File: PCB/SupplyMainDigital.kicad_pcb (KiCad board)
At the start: 2 copper layers, 84.8 x 57.5 mm, 103 parts, among them CON1 BARREL_JACK, P1 12V, P2 5V, P3 3V3, P4 GND, P5 PGM, P6 SERIAL, P7 I2C, P8 OUT, SW1 SW_PUSH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

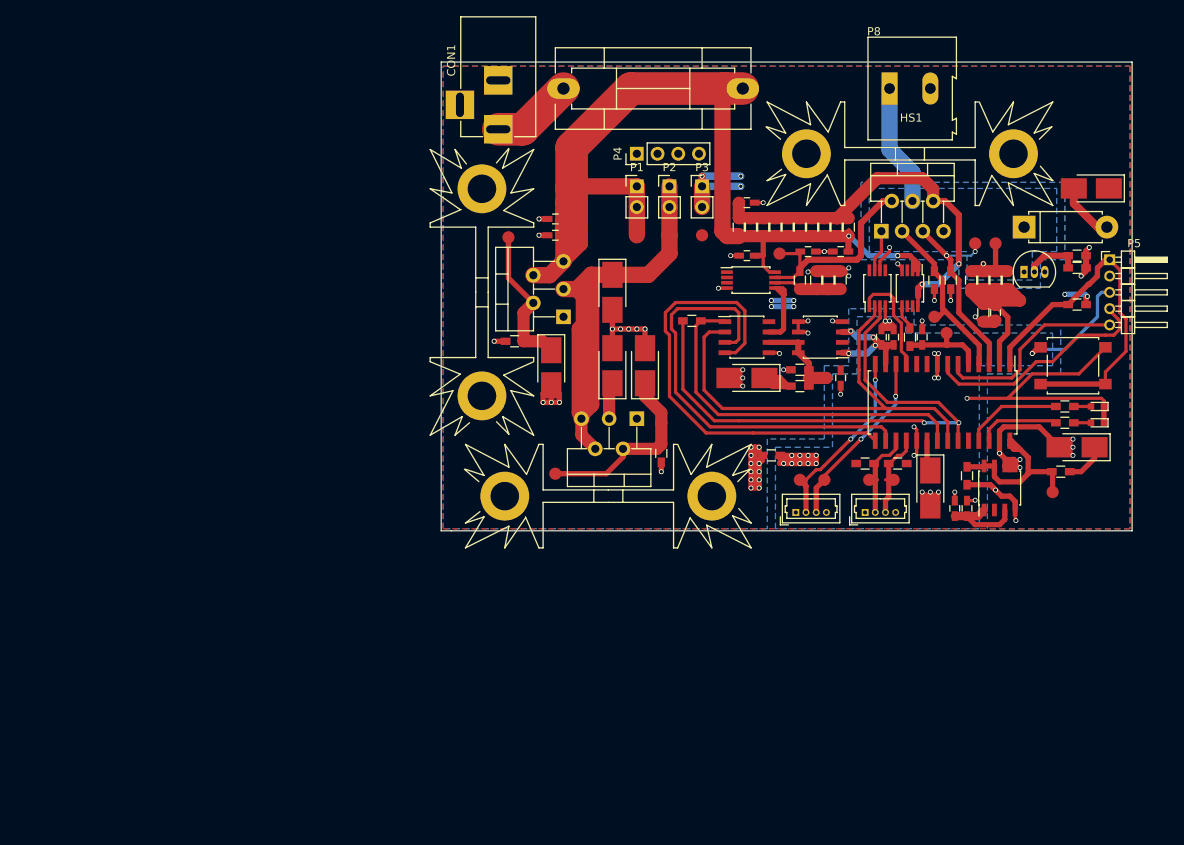
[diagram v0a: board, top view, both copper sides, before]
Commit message: component layout done
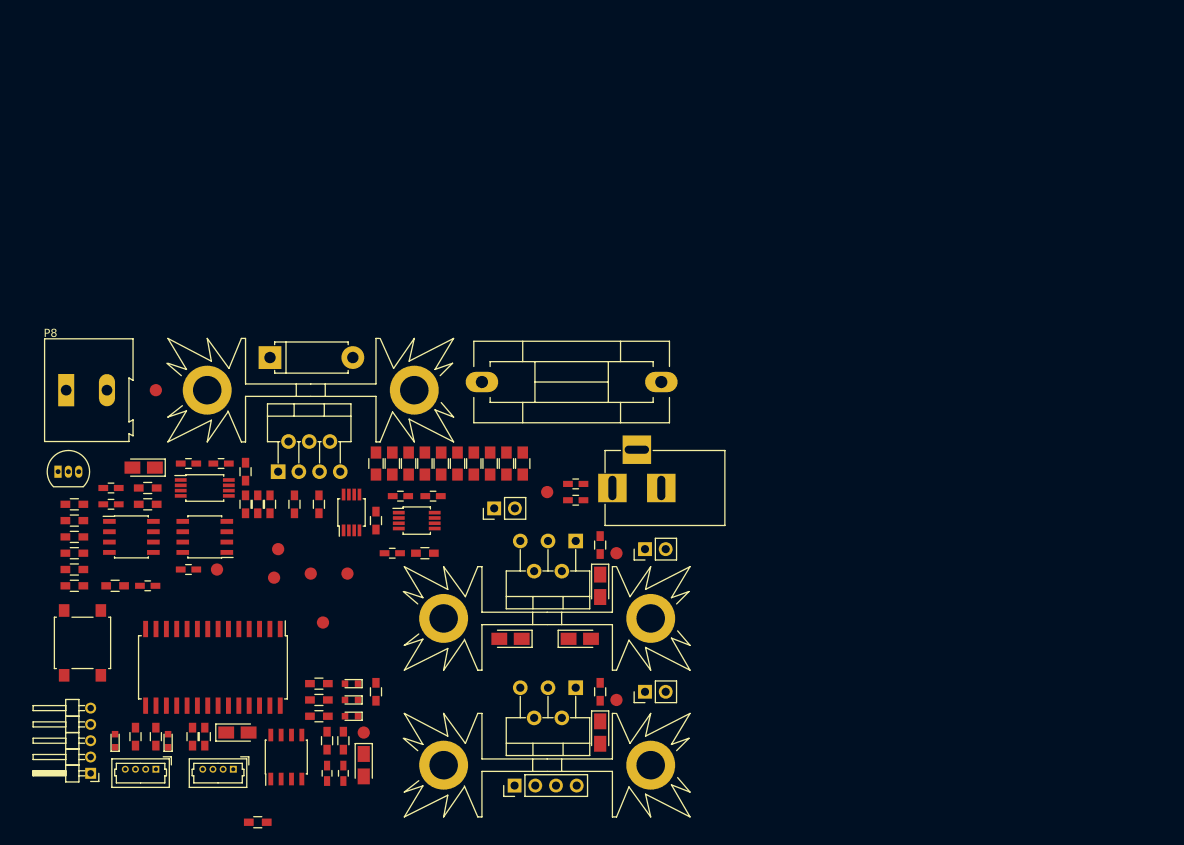
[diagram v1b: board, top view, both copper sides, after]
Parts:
- removed TP10, TP11, TP15, TP17, TP4, TP5: TEST, Measurement_Points:Measurement_Point_Round-SMD-Pad_Small
- removed eC20: 2.2µ **, Capacitors_Tantalum_SMD:CP_Tantalum_Case-B_EIA-3528-21_Hand
- added D4: LED, LEDs:LED_0603, F.Cu at (102.5, 95.0)
- added D5: LED, LEDs:LED_0603, F.Cu at (96.0, 95.0)
- added D6: LED, LEDs:LED_0603, F.Cu at (125.0, 88.0)
- added R38: 100, Resistors_SMD:R_0603_HandSoldering, F.Cu at (101.0, 94.5)
- added R39: 100, Resistors_SMD:R_0603_HandSoldering, F.Cu at (98.5, 94.5)
- added R40: 100, Resistors_SMD:R_0603_HandSoldering, F.Cu at (121.0, 88.0)
- C17, C18, C19, C20, C5, C6, C8: footprint Capacitors_Tantalum_SMD:CP_Tantalum_Case-B_EIA-3528-21_Hand -> Capacitors_Tantalum_SMD:CP_Tantalum_Case-A_EIA-3216-18_Reflow
- R14, R15, R16, R17, R18, R19, R20, R21, R22, R23: footprint Resistors_SMD:R_0603_HandSoldering -> Resistors_SMD:R_0805_HandSoldering
- TP1, TP2: value TEST -> Vref
- TP12: value TEST -> Vo+
- TP3: value TEST -> Set
- TP6: value TEST -> Vout
- TP7: value TEST -> Temp
- TP8: value TEST -> Imon
- TP9: value TEST -> Sense
- moved P5 140.0 mm to (93.0, 99.0), turned to 180 degrees
- moved R24 127.2 mm to (91.0, 68.0)
- moved R25 126.4 mm to (91.0, 66.0)
- moved SW1 126.2 mm to (92.0, 83.0), turned to 90 degrees
- moved U8 121.0 mm to (89.0, 62.0)
- moved R31 120.5 mm to (91.0, 76.0), turned to 0 degrees
- moved R29 117.9 mm to (91.0, 72.0), turned to 0 degrees
- moved R27 115.9 mm to (91.0, 70.0), turned to 0 degrees
- moved R30 115.6 mm to (91.0, 74.0), turned to 0 degrees
- moved R28 111.6 mm to (96.0, 76.0), turned to 0 degrees
- moved C14 109.3 mm to (100.0, 76.0), turned to 0 degrees
- moved P8 107.6 mm to (90.0, 52.0)
- moved C2 105.0 mm to (95.5, 66.0), turned to 0 degrees
- moved TP12 104.6 mm to (101.0, 52.0)
- moved C4 103.5 mm to (95.5, 64.0), turned to 0 degrees
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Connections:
- U5 pad 12: /SER_RX -> /SPI_CS_DAC
- U5 pad 14: /SER_TX -> /SPI_FS
- U5 pad 15: /SPI_FS -> /SER_RX
- U5 pad 16: /SPI_CS_DAC -> /SER_TX
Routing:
- net +12V: track 130.4 -> 0.00 mm, vias 2 -> 0
- net GNDA: track 119.6 -> 0.00 mm, vias 53 -> 0
- net GND: track 91.5 -> 0.00 mm, vias 25 -> 0
- net /SPI_SDI: track 69.8 -> 0.00 mm, vias 2 -> 0
- net +5V: track 60.6 -> 0.00 mm
- net /SPI_SCK: track 58.1 -> 0.00 mm
- net /SPI_FS: track 55.6 -> 0.00 mm
- net /SPI_CS_DAC: track 52.5 -> 0.00 mm
- net +3V3: track 50.1 -> 0.00 mm, vias 9 -> 0
- net /3081_IN: track 49.6 -> 0.00 mm, vias 2 -> 0
- net /SPI_SDO: track 45.3 -> 0.00 mm
- net /RESET: track 44.9 -> 0.00 mm
- net /PGM_PGED: track 28.6 -> 0.00 mm
- net /VO+: track 27.1 -> 0.00 mm, vias 2 -> 0
- net /VO_SENSE: track 26.0 -> 0.00 mm
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- removed copper zone on F.Cu, net +3V3
- removed copper zone on B.Cu, net /VO+
- removed copper zone on B.Cu, net GND
- removed copper zone on B.Cu, net GNDA
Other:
- board outline removed
- rule pad_to_mask_clearance: 0.2 -> 0
- rule trace_min: 0.1524 -> 0.2
- rule via_min_drill: 0.254 -> 0.3
- rule via_min_size: 0.381 -> 0.4

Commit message: Pcb layout V2 ready
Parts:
- TP12: value Vo+ -> Vout+
- TP6: value Vout -> Vo
- TP7: value Temp -> Sense
- TP8: value Imon -> Temp
- TP9: value Sense -> Imon
- U5: value dsPIC33EPXXXGP502 -> dsPIC33EP
- moved R36 32.9 mm to (90.5, 81.5), turned to 270 degrees
- moved SW1 31.6 mm to (123.6, 82.0), turned to 270 degrees
- moved TP6 19.3 mm to (96.5, 78.5)
- moved P4 17.4 mm to (132.0, 89.0)
- moved TP2 14.6 mm to (101.0, 61.5)
- moved TP3 14.1 mm to (109.5, 59.0)
- moved R5 13.7 mm to (118.6, 79.0), turned to 90 degrees
- moved C2 11.0 mm to (100.0, 76.0)
- moved C4 11.0 mm to (100.0, 74.0)
- moved TP7 10.7 mm to (128.2, 67.8)
- moved TP9 10.4 mm to (114.8, 71.0)
- moved TP8 10.1 mm to (118.0, 71.0)
- moved C1 7.00 mm to (117.0, 99.0)
- moved C3 7.00 mm to (115.0, 99.0)
- moved R1 7.00 mm to (115.0, 95.0)
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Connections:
- TP7 pad 1: /TEMP -> /VSENSE
- TP8 pad 1: /IMON -> /TEMP
- TP9 pad 1: /VSENSE -> /IMON
- U5 pad 3: /TEMP -> /VSENSE
- U5 pad 4: /IMON -> /TEMP
- U5 pad 5: /VSENSE -> /IMON
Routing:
- net +12V: track 0.00 -> 121.8 mm, vias 0 -> 6
- net GNDA: track 0.00 -> 105.0 mm, vias 0 -> 50
- net /VO+: track 0.00 -> 83.9 mm
- net /RESET: track 0.00 -> 82.0 mm, vias 0 -> 4
- net +5V: track 0.00 -> 81.0 mm
- net GND: track 0.00 -> 66.8 mm, vias 0 -> 24
- net /SPI_SCK: track 0.00 -> 54.3 mm, vias 0 -> 2
- net /SPI_SDO: track 0.00 -> 45.1 mm, vias 0 -> 2
- net /VO_SENSE: track 0.00 -> 39.8 mm, vias 0 -> 2
- net /SPI_CS_MCP: track 0.00 -> 32.9 mm, vias 0 -> 2
- net /VSENSE: track 0.00 -> 32.4 mm
- net /3081_IN: track 0.00 -> 32.2 mm, vias 0 -> 2
- net /SPI_SDI: track 0.00 -> 30.7 mm
- net /PGM_PGEC: track 0.00 -> 27.9 mm, vias 0 -> 2
- net /PGM_PGED: track 0.00 -> 26.1 mm, vias 0 -> 2
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- added copper zone on F.Cu, net +12V
- added copper zone on F.Cu, net +3V3
- added copper zone on F.Cu, net /Power/Pin
- added copper zone on B.Cu, net GND
- added copper zone on B.Cu, net GNDA
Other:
- board outline added: 79 x 57 mm
- rule trace_min: 0.2 -> 0.1524
- rule via_min_drill: 0.3 -> 0.254
- rule via_min_size: 0.4 -> 0.381
- board text added: "+ -"
- board text added: "1"
- board text added: "12V"
- board text added: "2"
- board text added: "3"
- board text added: "3V3"
- board text added: "4"
- board text added: "5V"
- board text added: "GND"
- board text added: "Gnd"
- board text added: "I2C"
- board text added: "I2C:"
- board text added: "PGEC"
- board text added: "PGED"
- board text added: "Program"
- board text added: "RESET"
- board text added: "RX"
- board text added: "Reset"
- board text added: "Rx"
- board text added: "TX"
- board text added: "Tx"
- board text added: "Uart"
- board text added: "Uart:"
- board text added: "scl"
- board text added: "sda"
